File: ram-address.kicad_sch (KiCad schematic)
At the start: 33 parts, among them SW3 SW_DIP_x08, U22 74HCT157, U23 74HCT157, U8 74HCT173, U9 74HCT173

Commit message: ram address 7 led now uses the arbitrated signal
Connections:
- net RAM_ADDRESS_7: no longer R11.1
- new net ARB_RAM_ADDRESS_7: R11.1
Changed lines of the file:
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@@
   (junction (at 74.93 193.04) (diameter 0) (color 0 0 0 0)
   )
-  (junction (at 64.77 168.91) (diameter 0) (color 0 0 0 0)
-  )
   (junction (at 21.59 102.87) (diameter 0) (color 0 0 0 0)
   )
@@
     (stroke (width 0) (type default))
   )
+  (wire (pts (xy 64.77 172.72) (xy 64.77 175.26))
+    (stroke (width 0) (type default))
+  )
   (wire (pts (xy 185.42 158.75) (xy 129.54 158.75))
     (stroke (width 0) (type default))
@@
     (stroke (width 0) (type default))
   )
-  (wire (pts (xy 64.77 168.91) (xy 64.77 175.26))
-    (stroke (width 0) (type default))
-  )
   (wire (pts (xy 110.49 50.8) (xy 110.49 54.61))
     (stroke (width 0) (type default))
@@
   )
   (wire (pts (xy 261.62 147.32) (xy 190.5 147.32))
+    (stroke (width 0) (type default))
+  )
+  (wire (pts (xy 43.18 172.72) (xy 64.77 172.72))
     (stroke (width 0) (type default))
   )
@@
     (effects (font (size 1.27 1.27)) (justify left))
   )
+  (hierarchical_label "ARB_RAM_ADDRESS_7" (shape input) (at 43.18 172.72 180) (fields_autoplaced)
+    (effects (font (size 1.27 1.27)) (justify right))
+  )
   (hierarchical_label "BUS_5" (shape bidirectional) (at 261.62 34.29 0) (fields_autoplaced)

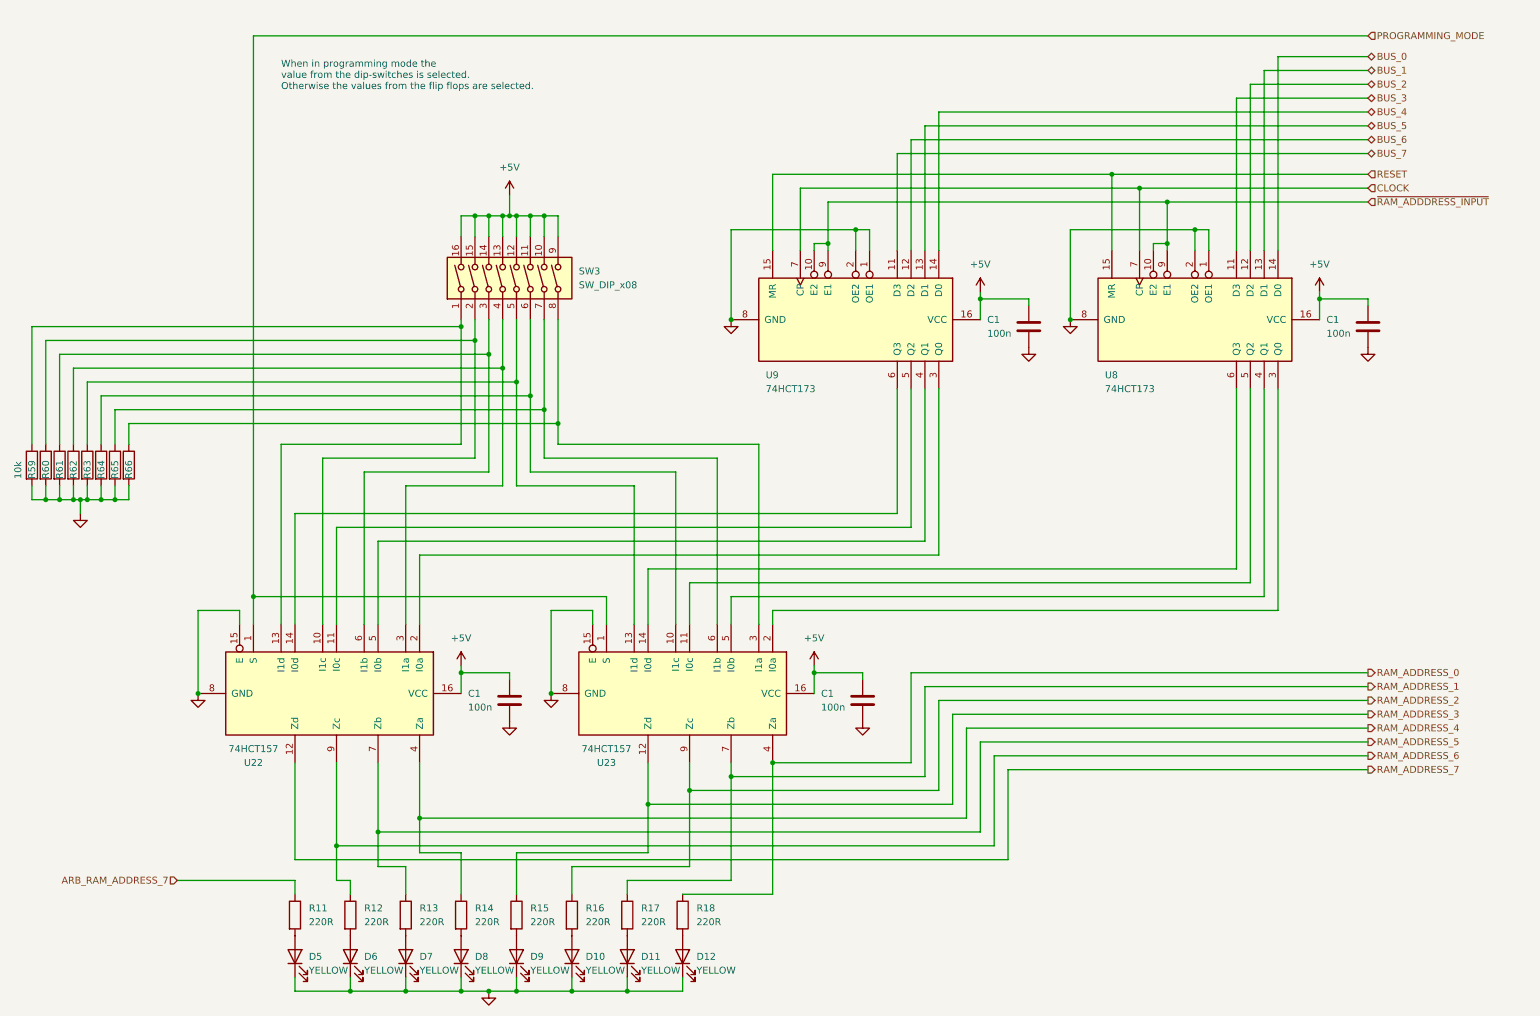
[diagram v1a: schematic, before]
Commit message: Fixed out instructions, no CE.  Added note about RESET line in RaI
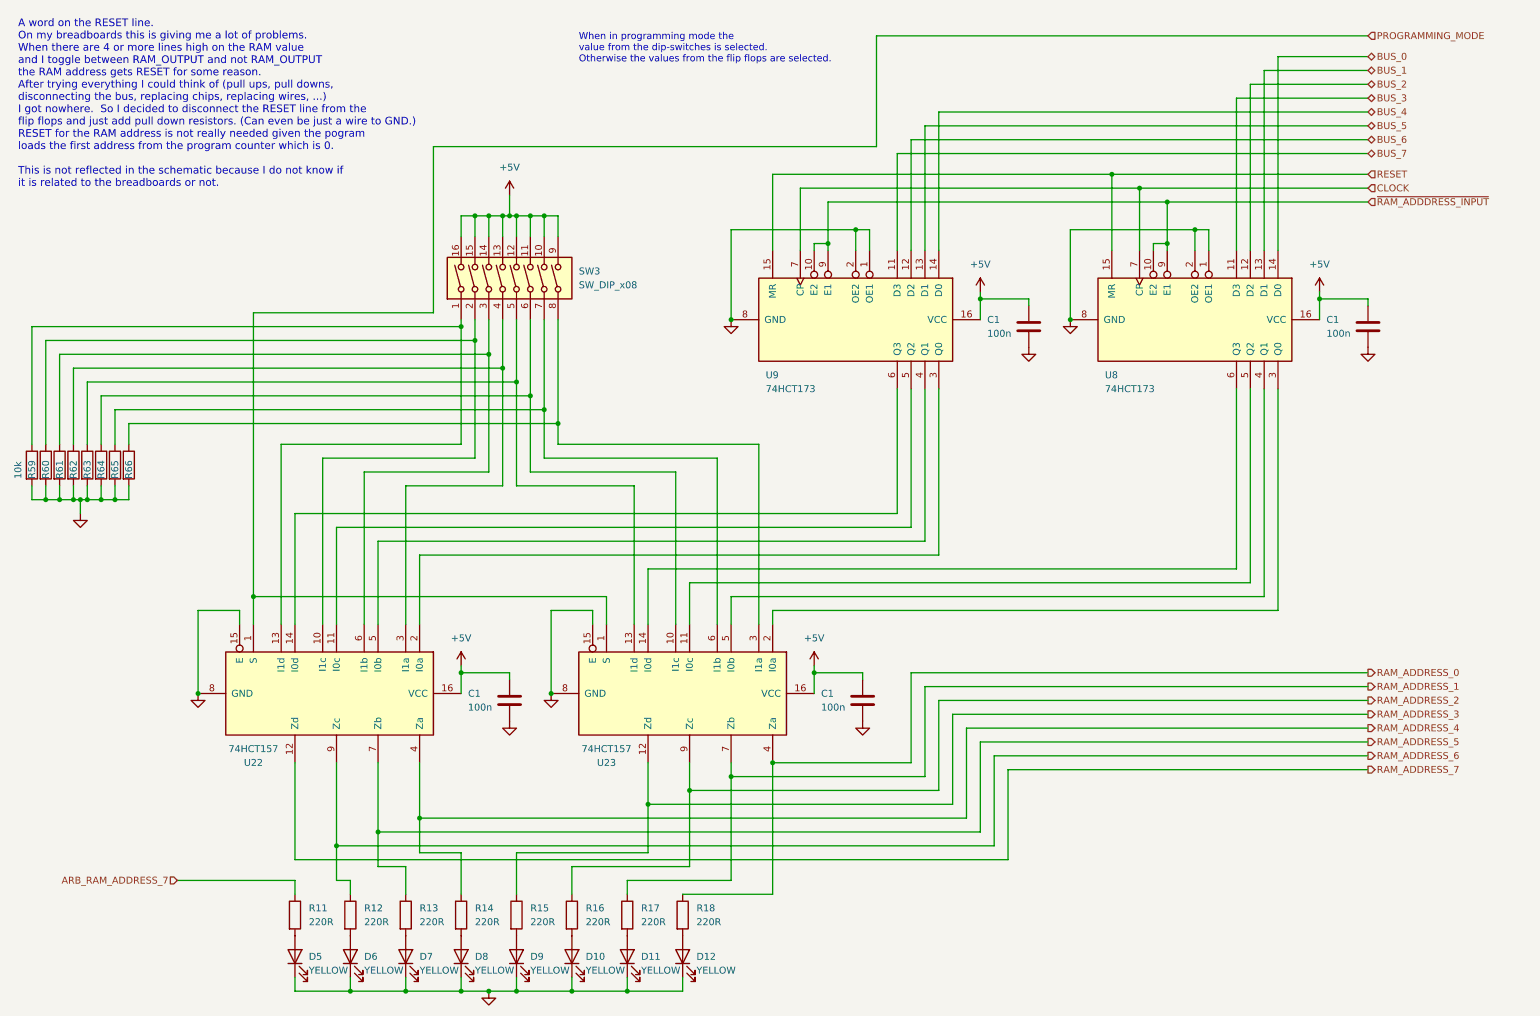
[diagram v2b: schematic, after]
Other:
- note added: "A word on the RESET line. On my breadboards this is giving me a lot of problems. When there are 4 or more lines high on the RAM value and I toggle between RAM_OUTPUT and not RAM_OUTPUT the RAM address gets RESET for some reason. After trying everything I could think of (pull ups, pull downs, disconnecting the bus, replacing chips, replacing wires, ...) I got nowhere. So I decided to disconnect th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"
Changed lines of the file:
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@@
   (junction (at 100.33 50.8) (diameter 0) (color 0 0 0 0)
   )
+  (junction (at 24.13 102.87) (diameter 0) (color 0 0 0 0)
+  )
+  (junction (at 25.4 102.87) (diameter 0) (color 0 0 0 0)
+  )
+  (junction (at 29.21 102.87) (diameter 0) (color 0 0 0 0)
+  )
+  (junction (at 252.73 66.04) (diameter 0) (color 0 0 0 0)
+  )
+  (junction (at 31.75 102.87) (diameter 0) (color 0 0 0 0)
+  )
+  (junction (at 107.95 50.8) (diameter 0) (color 0 0 0 0)
+  )
+  (junction (at 100.33 193.04) (diameter 0) (color 0 0 0 0)
+  )
+  (junction (at 80.01 163.83) (diameter 0) (color 0 0 0 0)
+  )
+  (junction (at 105.41 50.8) (diameter 0) (color 0 0 0 0)
+  )
+  (junction (at 207.01 69.85) (diameter 0) (color 0 0 0 0)
+  )
+  (junction (at 72.39 166.37) (diameter 0) (color 0 0 0 0)
+  )
+  (junction (at 19.05 102.87) (diameter 0) (color 0 0 0 0)
+  )
+  (junction (at 105.41 81.28) (diameter 0) (color 0 0 0 0)
+  )
+  (junction (at 167.64 53.34) (diameter 0) (color 0 0 0 0)
+  )
+  (junction (at 97.79 50.8) (diameter 0) (color 0 0 0 0)
+  )
+  (junction (at 102.87 50.8) (diameter 0) (color 0 0 0 0)
+  )
+  (junction (at 111.76 138.43) (diameter 0) (color 0 0 0 0)
+  )
+  (junction (at 162.56 55.88) (diameter 0) (color 255 0 0 1)
+  )
+  (junction (at 219.71 45.72) (diameter 0) (color 255 0 0 1)
+  )
+  (junction (at 85.09 193.04) (diameter 0) (color 0 0 0 0)
+  )
+  (junction (at 224.79 55.88) (diameter 0) (color 255 0 0 1)
+  )
+  (junction (at 152.4 151.13) (diameter 0) (color 0 0 0 0)
+  )
+  (junction (at 160.02 134.62) (diameter 0) (color 0 0 0 0)
+  )
+  (junction (at 190.5 66.04) (diameter 0) (color 0 0 0 0)
+  )
+  (junction (at 26.67 102.87) (diameter 0) (color 0 0 0 0)
+  )
+  (junction (at 100.33 76.2) (diameter 0) (color 0 0 0 0)
+  )
+  (junction (at 107.95 83.82) (diameter 0) (color 0 0 0 0)
+  )
+  (junction (at 125.73 193.04) (diameter 0) (color 0 0 0 0)
+  )
+  (junction (at 95.25 71.12) (diameter 0) (color 0 0 0 0)
+  )
+  (junction (at 95.25 134.62) (diameter 0) (color 0 0 0 0)
+  )
+  (junction (at 105.41 193.04) (diameter 0) (color 0 0 0 0)
+  )
+  (junction (at 214.63 43.18) (diameter 0) (color 255 0 0 1)
+  )
+  (junction (at 74.93 193.04) (diameter 0) (color 0 0 0 0)
+  )
+  (junction (at 21.59 102.87) (diameter 0) (color 0 0 0 0)
+  )
+  (junction (at 102.87 78.74) (diameter 0) (color 0 0 0 0)
+  )
+  (junction (at 137.16 156.21) (diameter 0) (color 0 0 0 0)
+  )
+  (junction (at 113.03 88.9) (diameter 0) (color 0 0 0 0)
+  )
+  (junction (at 110.49 50.8) (diameter 0) (color 0 0 0 0)
+  )
+  (junction (at 104.14 50.8) (diameter 0) (color 0 0 0 0)
+  )
+  (junction (at 144.78 69.85) (diameter 0) (color 0 0 0 0)
+  )
+  (junction (at 229.87 53.34) (diameter 0) (color 0 0 0 0)
+  )
+  (junction (at 115.57 193.04) (diameter 0) (color 0 0 0 0)
+  )
   (junction (at 57.15 120.65) (diameter 0) (color 255 0 0 1)
   )
-  (junction (at 24.13 102.87) (diameter 0) (color 0 0 0 0)
-  )
-  (junction (at 25.4 102.87) (diameter 0) (color 0 0 0 0)
-  )
-  (junction (at 29.21 102.87) (diameter 0) (color 0 0 0 0)
-  )
-  (junction (at 252.73 66.04) (diameter 0) (color 0 0 0 0)
-  )
-  (junction (at 31.75 102.87) (diameter 0) (color 0 0 0 0)
-  )
-  (junction (at 107.95 50.8) (diameter 0) (color 0 0 0 0)
-  )
-  (junction (at 100.33 193.04) (diameter 0) (color 0 0 0 0)
-  )
-  (junction (at 80.01 163.83) (diameter 0) (color 0 0 0 0)
-  )
-  (junction (at 105.41 50.8) (diameter 0) (color 0 0 0 0)
-  )
-  (junction (at 207.01 69.85) (diameter 0) (color 0 0 0 0)
-  )
-  (junction (at 72.39 166.37) (diameter 0) (color 0 0 0 0)
-  )
-  (junction (at 19.05 102.87) (diameter 0) (color 0 0 0 0)
-  )
-  (junction (at 105.41 81.28) (diameter 0) (color 0 0 0 0)
-  )
-  (junction (at 167.64 53.34) (diameter 0) (color 0 0 0 0)
-  )
-  (junction (at 97.79 50.8) (diameter 0) (color 0 0 0 0)
-  )
-  (junction (at 102.87 50.8) (diameter 0) (color 0 0 0 0)
-  )
-  (junction (at 111.76 138.43) (diameter 0) (color 0 0 0 0)
-  )
-  (junction (at 162.56 55.88) (diameter 0) (color 255 0 0 1)
-  )
-  (junction (at 219.71 45.72) (diameter 0) (color 255 0 0 1)
-  )
-  (junction (at 85.09 193.04) (diameter 0) (color 0 0 0 0)
-  )
-  (junction (at 224.79 55.88) (diameter 0) (color 255 0 0 1)
-  )
-  (junction (at 152.4 151.13) (diameter 0) (color 0 0 0 0)
-  )
-  (junction (at 160.02 134.62) (diameter 0) (color 0 0 0 0)
-  )
-  (junction (at 190.5 66.04) (diameter 0) (color 0 0 0 0)
-  )
-  (junction (at 26.67 102.87) (diameter 0) (color 0 0 0 0)
-  )
-  (junction (at 100.33 76.2) (diameter 0) (color 0 0 0 0)
-  )
-  (junction (at 107.95 83.82) (diameter 0) (color 0 0 0 0)
-  )
-  (junction (at 125.73 193.04) (diameter 0) (color 0 0 0 0)
-  )
-  (junction (at 95.25 71.12) (diameter 0) (color 0 0 0 0)
-  )
-  (junction (at 95.25 134.62) (diameter 0) (color 0 0 0 0)
-  )
-  (junction (at 105.41 193.04) (diameter 0) (color 0 0 0 0)
-  )
-  (junction (at 214.63 43.18) (diameter 0) (color 255 0 0 1)
-  )
-  (junction (at 74.93 193.04) (diameter 0) (color 0 0 0 0)
-  )
-  (junction (at 21.59 102.87) (diameter 0) (color 0 0 0 0)
-  )
-  (junction (at 102.87 78.74) (diameter 0) (color 0 0 0 0)
-  )
-  (junction (at 137.16 156.21) (diameter 0) (color 0 0 0 0)
-  )
-  (junction (at 113.03 88.9) (diameter 0) (color 0 0 0 0)
-  )
-  (junction (at 110.49 50.8) (diameter 0) (color 0 0 0 0)
-  )
-  (junction (at 104.14 50.8) (diameter 0) (color 0 0 0 0)
-  )
-  (junction (at 144.78 69.85) (diameter 0) (color 0 0 0 0)
-  )
-  (junction (at 229.87 53.34) (diameter 0) (color 0 0 0 0)
-  )
-  (junction (at 115.57 193.04) (diameter 0) (color 0 0 0 0)
-  )
   (junction (at 224.79 48.26) (diameter 0) (color 255 0 0 1)
   )
@@
     (stroke (width 0) (type default))
   )
-  (wire (pts (xy 57.15 17.78) (xy 261.62 17.78))
-    (stroke (width 0) (type default) (color 255 0 0 1))
-  )
   (wire (pts (xy 95.25 54.61) (xy 95.25 50.8))
     (stroke (width 0) (type default))
@@
     (stroke (width 0) (type default))
   )
+  (wire (pts (xy 261.62 17.78) (xy 171.45 17.78))
+    (stroke (width 0) (type default) (color 255 0 0 1))
+  )
   (wire (pts (xy 105.41 193.04) (xy 115.57 193.04))
     (stroke (width 0) (type default))
@@
     (stroke (width 0) (type default))
   )
+  (wire (pts (xy 90.17 38.1) (xy 90.17 68.58))
+    (stroke (width 0) (type default) (color 255 0 0 1))
+  )
   (wire (pts (xy 111.76 123.19) (xy 111.76 138.43))
     (stroke (width 0) (type default))
@@
     (stroke (width 0) (type default) (color 0 0 255 1))
   )
-  (wire (pts (xy 57.15 17.78) (xy 57.15 120.65))
-    (stroke (width 0) (type default) (color 255 0 0 1))
-  )
   (wire (pts (xy 26.67 81.28) (xy 105.41 81.28))
     (stroke (width 0) (type default))
@@
     (stroke (width 0) (type default) (color 255 0 0 1))
   )
+  (wire (pts (xy 171.45 38.1) (xy 90.17 38.1))
+    (stroke (width 0) (type default) (color 255 0 0 1))
+  )
   (wire (pts (xy 261.62 142.24) (xy 185.42 142.24))
     (stroke (width 0) (type default))
@@
     (stroke (width 0) (type default))
   )
+  (wire (pts (xy 171.45 17.78) (xy 171.45 38.1))
+    (stroke (width 0) (type default) (color 255 0 0 1))
+  )
   (wire (pts (xy 64.77 193.04) (xy 64.77 190.5))
     (stroke (width 0) (type default))
@@
     (stroke (width 0) (type default))
   )
+  (wire (pts (xy 90.17 68.58) (xy 57.15 68.58))
+    (stroke (width 0) (type default) (color 255 0 0 1))
+  )
   (wire (pts (xy 80.01 163.83) (xy 190.5 163.83))
     (stroke (width 0) (type default))
@@
     (stroke (width 0) (type default))
   )
+  (wire (pts (xy 57.15 68.58) (xy 57.15 120.65))
+    (stroke (width 0) (type default) (color 255 0 0 1))
+  )
   (wire (pts (xy 102.87 50.8) (xy 102.87 54.61))
     (stroke (width 0) (type default))
@@
     (stroke (width 0) (type default))
   )
+  (text "A word on the RESET line.\nOn my breadboards this is giving me a lot of problems.\nWhen there are 4 or more lines high on the RAM value\nand I toggle between RAM_OUTPUT and not RAM_OUTPUT\nthe RAM address gets RESET for some reason.\nAfter trying everything I could think of (pull ups, pull downs,\ndisconnecting the bus, replacing chips, replacing wires, ...)\nI got nowhere.  So I decided to disconnect the RESET line from the\nflip flops and just add pull down resistors. (Can even be just a wire to GND.)\nRESET for the RAM address is not really needed given the pogram\nloads the first address from the program counter which is 0.\n\nThis is not reflected in the schematic because I do not know if\nit is related to the breadboards or not."
+    (at 13.97 45.72 0)
+    (effects (font (size 1.4 1.4) (color 0 0 132 1)) (justify left bottom))
+  )
   (text "When in programming mode the\nvalue from the dip-switches is selected.\nOtherwise the values from the flip flops are selected."
-    (at 62.23 27.94 0)
+    (at 116.84 22.86 0)
     (effects (font (size 1.27 1.27)) (justify left bottom))
   )

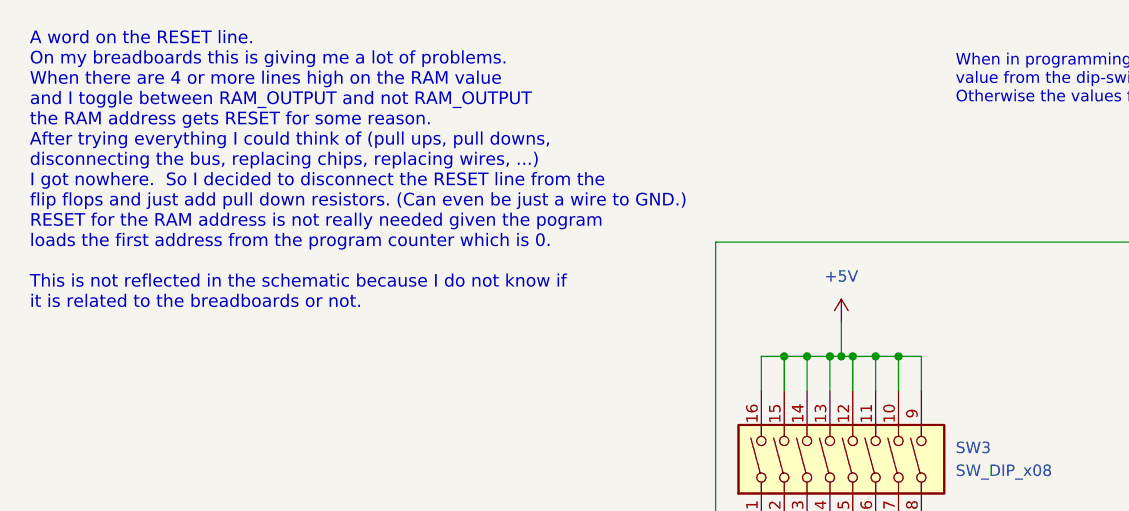
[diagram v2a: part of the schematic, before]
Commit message: added stack and x register.  Added logic for stack_address so ram address 7 gets passes and ram address 8 is high
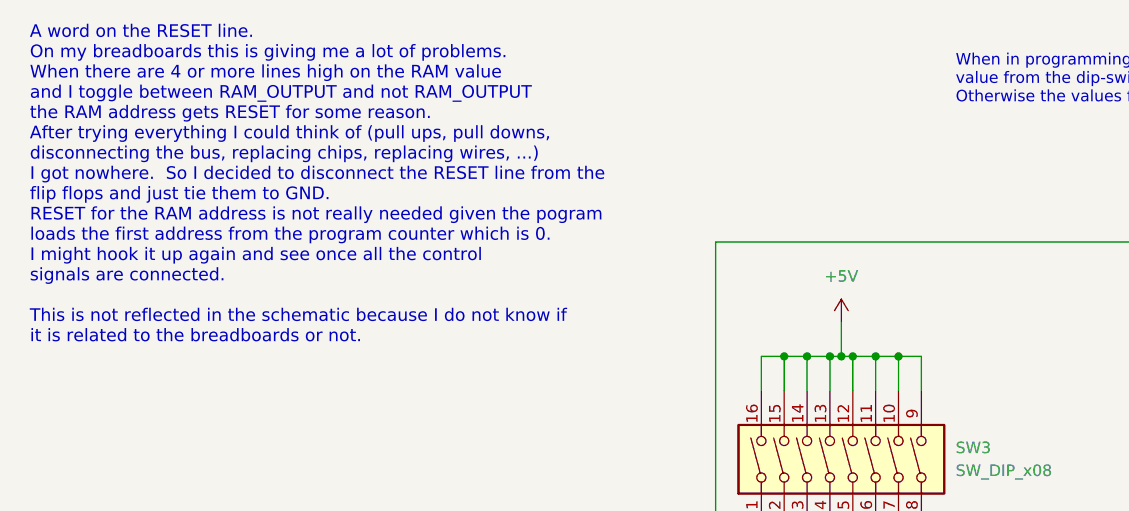
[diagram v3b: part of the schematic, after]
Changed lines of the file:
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@@
     (stroke (width 0) (type default))
   )
-  (text "A word on the RESET line.\nOn my breadboards this is giving me a lot of problems.\nWhen there are 4 or more lines high on the RAM value\nand I toggle between RAM_OUTPUT and not RAM_OUTPUT\nthe RAM address gets RESET for some reason.\nAfter trying everything I could think of (pull ups, pull downs,\ndisconnecting the bus, replacing chips, replacing wires, ...)\nI got nowhere.  So I decided to disconnect the RESET line from the\nflip flops and just add pull down resistors. (Can even be just a wire to GND.)\nRESET for the RAM address is not really needed given the pogram\nloads the first address from the program counter which is 0.\n\nThis is not reflected in the schematic because I do not know if\nit is related to the breadboards or not."
-    (at 13.97 45.72 0)
+  (text "A word on the RESET line.\nOn my breadboards this is giving me a lot of problems.\nWhen there are 4 or more lines high on the RAM value\nand I toggle between RAM_OUTPUT and not RAM_OUTPUT\nthe RAM address gets RESET for some reason.\nAfter trying everything I could think of (pull ups, pull downs,\ndisconnecting the bus, replacing chips, replacing wires, ...)\nI got nowhere.  So I decided to disconnect the RESET line from the\nflip flops and just tie them to GND.\nRESET for the RAM address is not really needed given the pogram\nloads the first address from the program counter which is 0.\nI might hook it up again and see once all the control \nsignals are connected.\n\nThis is not reflected in the schematic because I do not know if\nit is related to the breadboards or not."
+    (at 13.97 49.53 0)
     (effects (font (size 1.4 1.4) (color 0 0 132 1)) (justify left bottom))
   )
